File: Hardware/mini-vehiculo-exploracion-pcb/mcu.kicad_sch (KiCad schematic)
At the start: 20 parts, among them J2 USB_C_Receptacle_USB2.0_16P, SW1 SW_Push, SW2 SW_Push

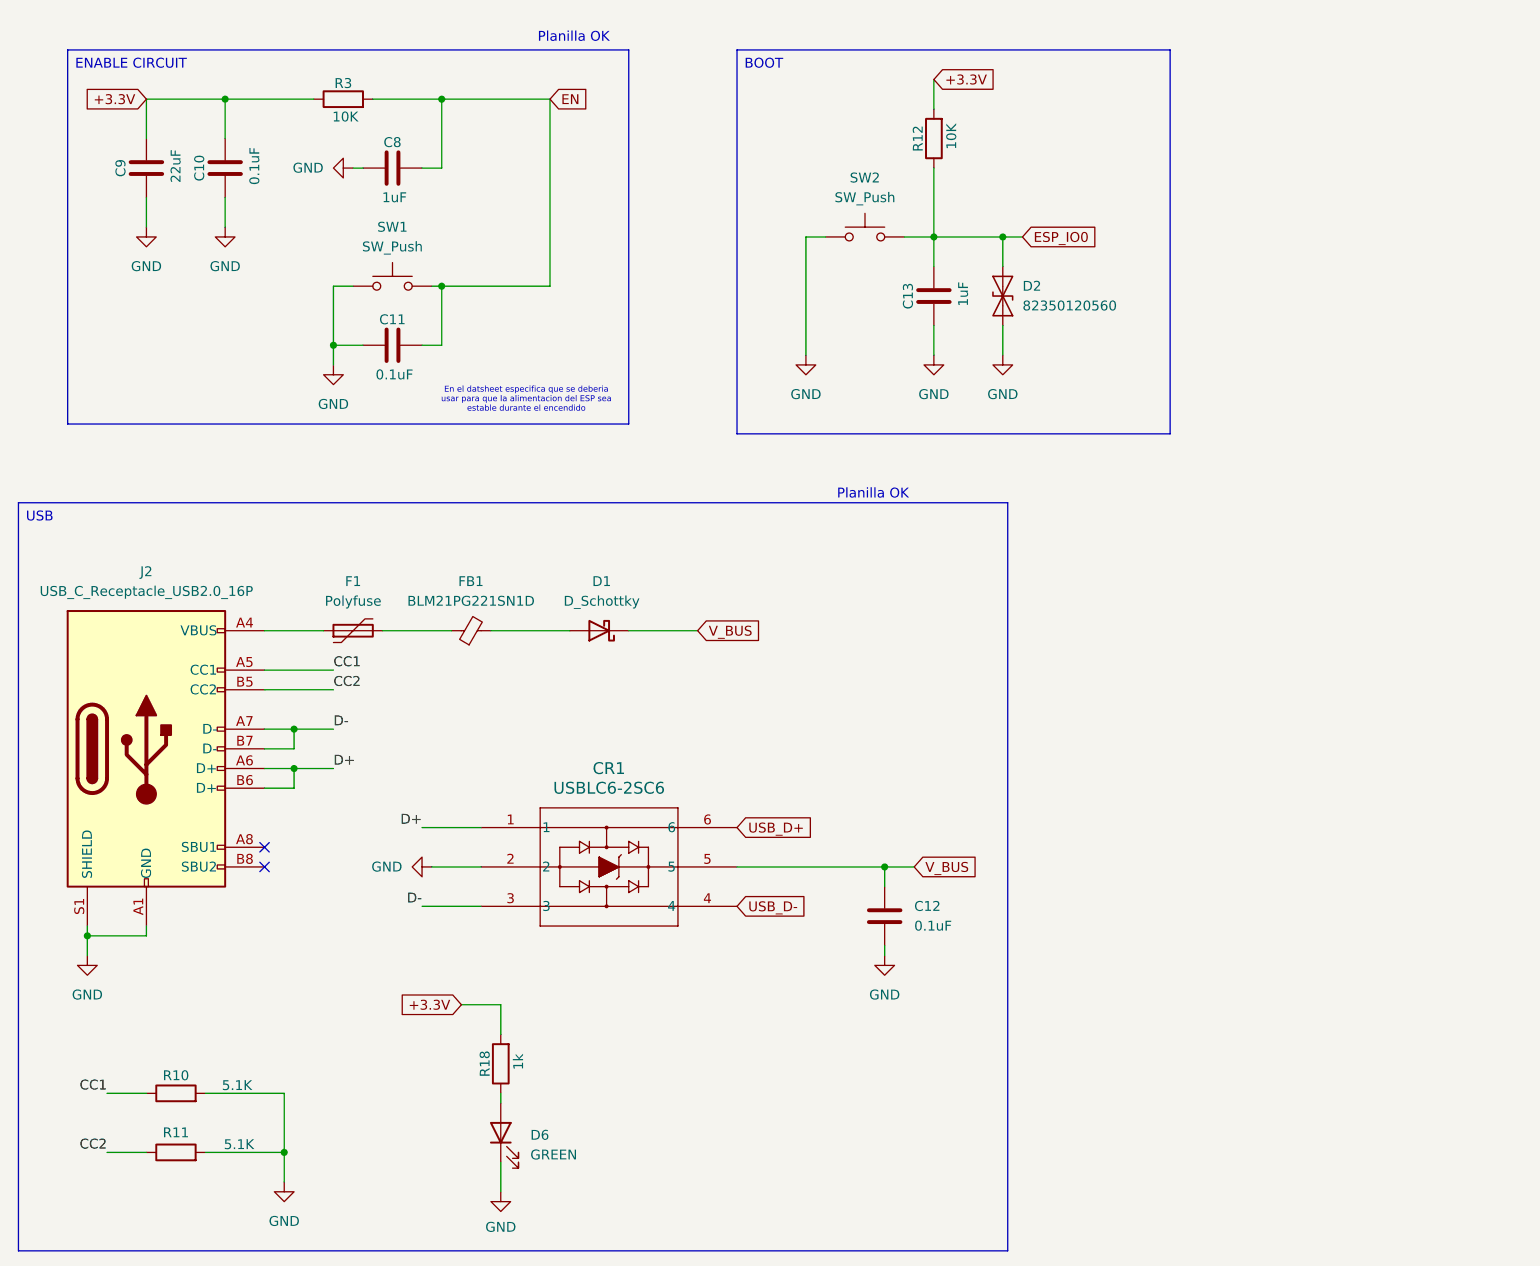
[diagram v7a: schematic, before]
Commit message: Add footprints
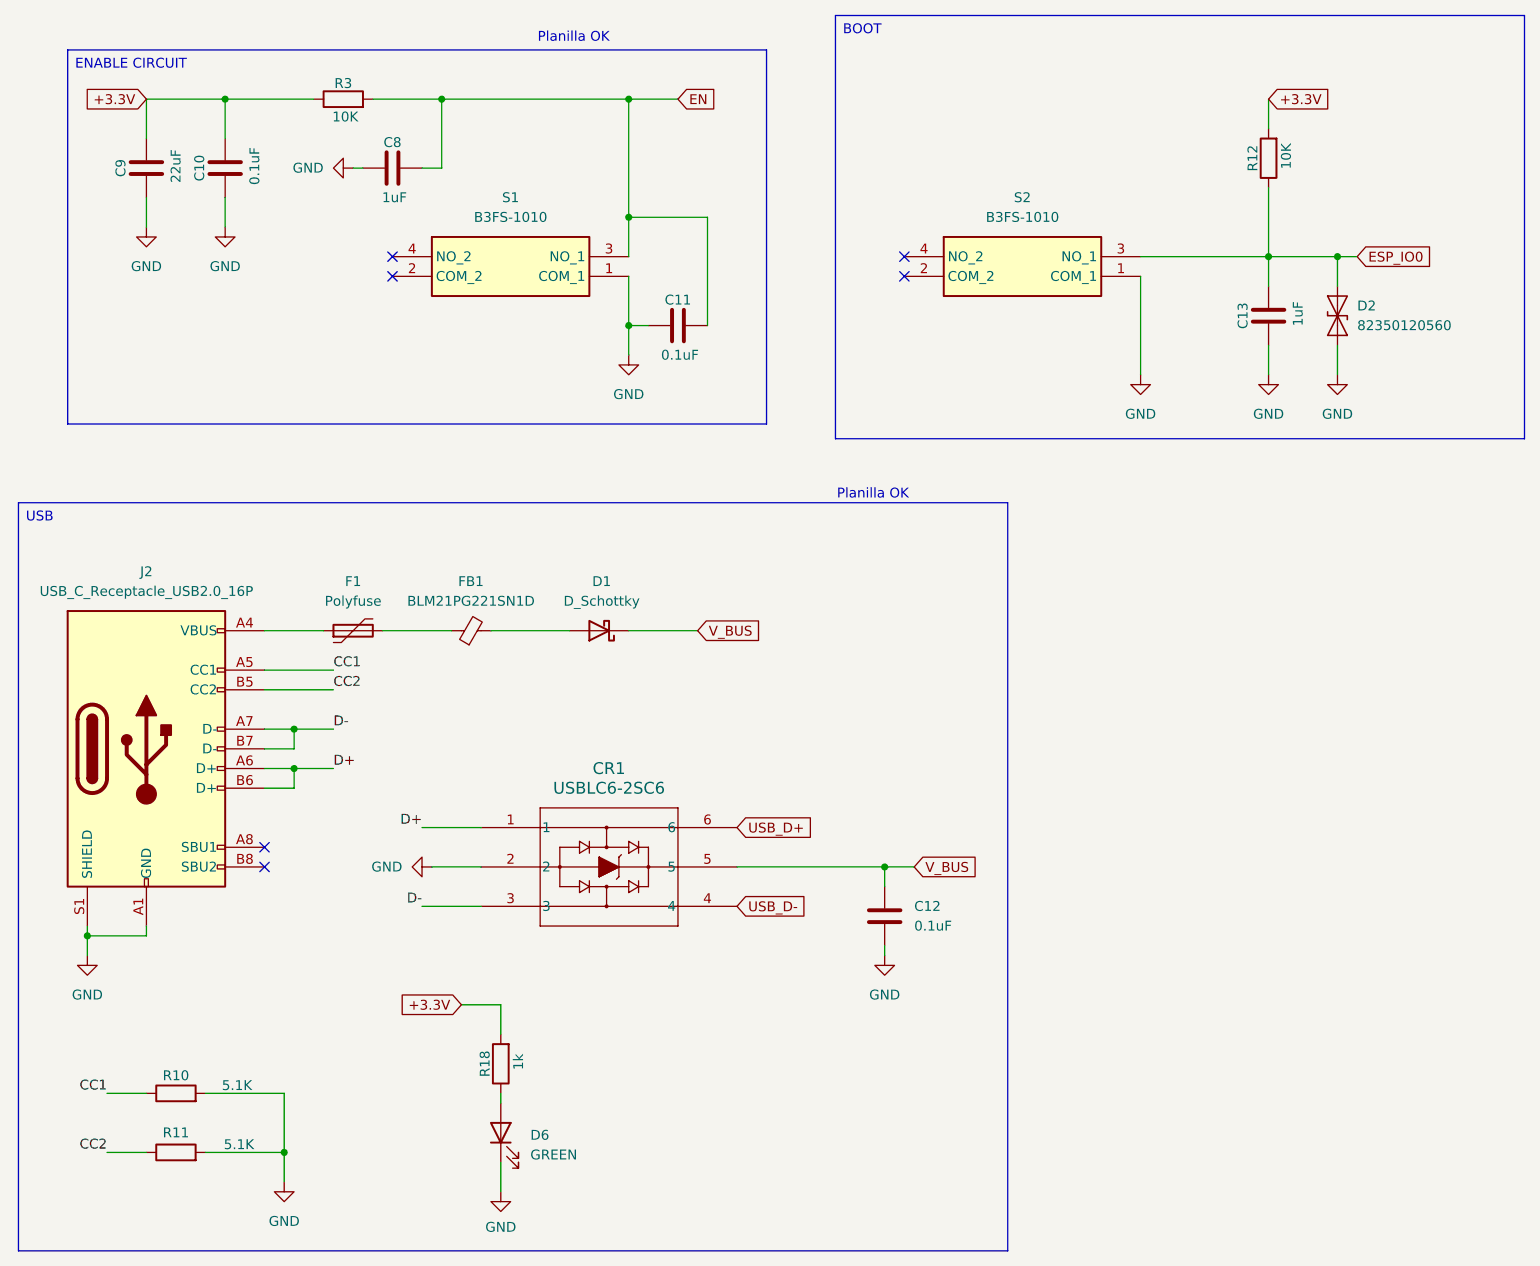
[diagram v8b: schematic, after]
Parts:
- removed SW1, SW2: SW_Push, B3FS-1010:B3FS-1000P, symbol Switch:SW_Push
- added S1, S2: B3FS-1010, B3FS-1010:B3FS-1000P, symbol B3FS-1010:B3FS-1010
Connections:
- net EN: now also S1.3 (NO_1)
- net ESP_IO0: now also S2.3 (NO_1)
- net GND: now also S1.1 (COM_1), S2.1 (COM_1)
- no-connect marks 2 -> 6
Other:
- note removed: "En el datsheet especifica que se deberia usar para que la alimentacion del ESP sea estable durante el encendido"
- moved on the sheet: C11, C13, D2, R12
